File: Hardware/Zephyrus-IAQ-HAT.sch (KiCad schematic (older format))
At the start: 8 parts, among them J1 Conn_02x20_Odd_Even__Rpi, J2 USART, U3 BSS138

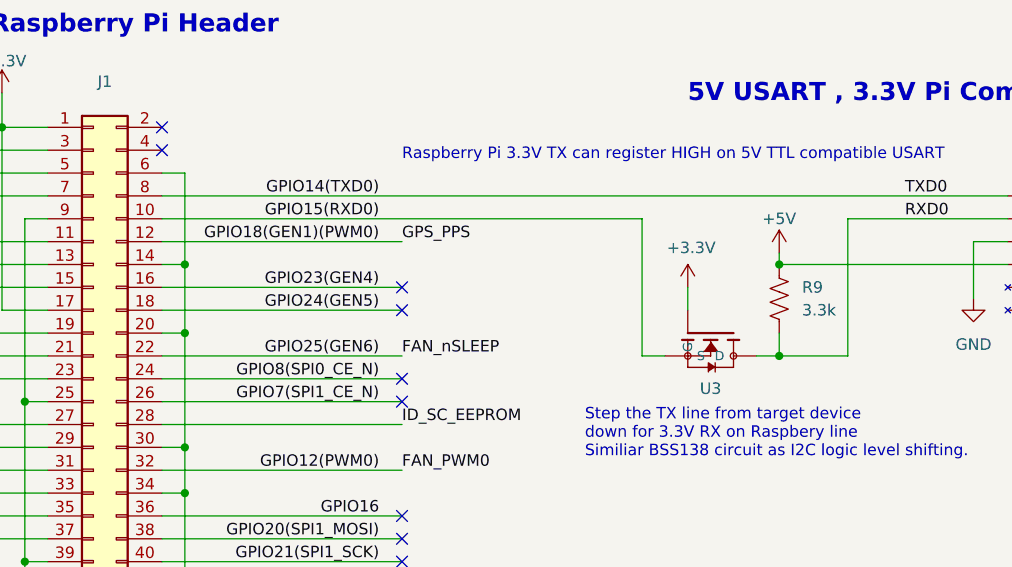
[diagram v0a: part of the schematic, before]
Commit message: Add Pull-Up to UART line.
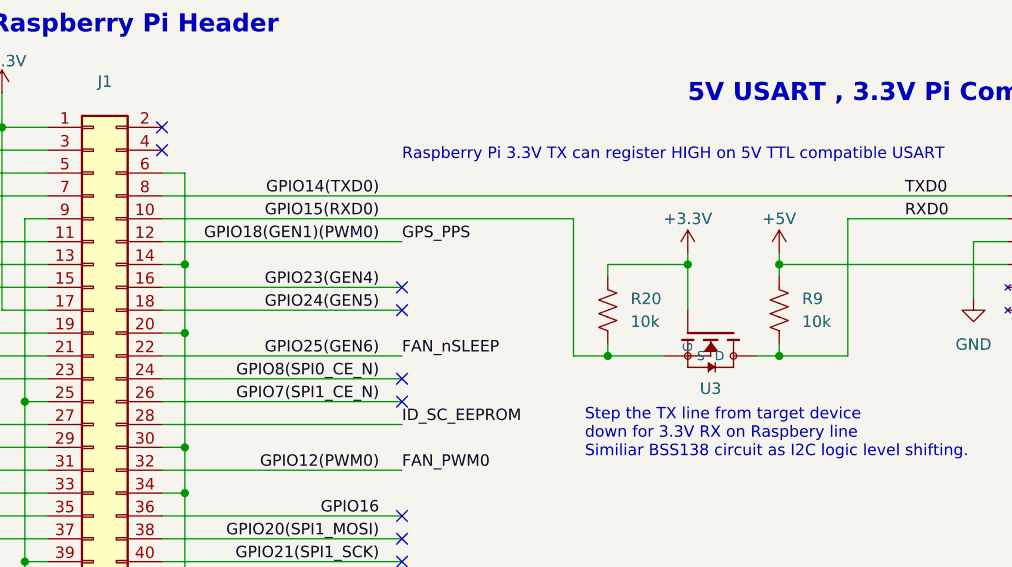
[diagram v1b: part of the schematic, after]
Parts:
- added R20: 10k, Resistor_SMD:R_0805_2012Metric, symbol zephyrus_iaq:R_US
- R9: value 3.3k -> 10k
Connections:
- wire segments 81 -> 87
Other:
- moved on the sheet: R9
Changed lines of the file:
@@
 Text Notes 2000 750  0    79   ~ 16
 Raspberry Pi Header
-Wire Wire Line
-	5050 1850 5050 1950
 $Comp
 L zephyrus_iaq:BSS138 U?
@@
 L zephyrus_iaq:R_US R?
 U 1 1 5DE9F972
-P 5450 1900
+P 5450 1950
 AR Path="/5DB861AF/5DE9F972" Ref="R?"  Part="1"
 AR Path="/5DE9F972" Ref="R9"  Part="1"
-F 0 "R9" H 5550 1950 50  0000 L CNN
-F 1 "3.3k" H 5550 1850 50  0000 L CNN
-F 2 "Resistor_SMD:R_0805_2012Metric" V 5490 1890 50  0001 C CNN
-F 3 "~" H 5450 1900 50  0001 C CNN
-	1    5450 1900
-	1    0    0    -1
-$EndComp
-Wire Wire Line
-	4850 2150 4950 2150
-Wire Wire Line
-	5350 2150 5450 2150
-Wire Wire Line
-	5450 2150 5450 2050
+F 0 "R9" H 5550 2000 50  0000 L CNN
+F 1 "10k" H 5550 1900 50  0000 L CNN
+F 2 "Resistor_SMD:R_0805_2012Metric" V 5490 1940 50  0001 C CNN
+F 3 "~" H 5450 1950 50  0001 C CNN
+	1    5450 1950
+	1    0    0    -1
+$EndComp
 $Comp
 L zephyrus_iaq:+3.3V #PWR?
 U 1 1 5DE9F969
-P 5050 1850
+P 5050 1700
 AR Path="/5DB861AF/5DE9F969" Ref="#PWR?"  Part="1"
 AR Path="/5DE9F969" Ref="#PWR0109"  Part="1"
-F 0 "#PWR0109" H 5050 1700 50  0001 C CNN
-F 1 "+3.3V" H 5065 2023 50  0000 C CNN
-F 2 "" H 5050 1850 50  0001 C CNN
-F 3 "" H 5050 1850 50  0001 C CNN
-	1    5050 1850
+F 0 "#PWR0109" H 5050 1550 50  0001 C CNN
+F 1 "+3.3V" H 5050 1850 50  0000 C CNN
+F 2 "" H 5050 1700 50  0001 C CNN
+F 3 "" H 5050 1700 50  0001 C CNN
+	1    5050 1700
 	1    0    0    -1
 $EndComp
@@
 $EndComp
 Wire Wire Line
-	5450 2150 5750 2150
-Wire Wire Line
 	5750 2150 5750 1550
-Connection ~ 5450 2150
 Wire Wire Line
 	5750 1550 6450 1550
@@
 Wire Wire Line
 	5450 1700 5450 1750
-Connection ~ 5450 1750
-Wire Wire Line
-	4850 1550 4850 2150
-Wire Wire Line
-	2750 1550 4850 1550
 Wire Wire Line
 	2750 1450 6450 1450
@@
 	1    0    0    -1
 $EndComp
+$Comp
+L zephyrus_iaq:R_US R?
+U 1 1 5DD3B4E5
+P 4700 1950
+AR Path="/5DB861AF/5DD3B4E5" Ref="R?"  Part="1"
+AR Path="/5DD3B4E5" Ref="R20"  Part="1"
+F 0 "R20" H 4800 2000 50  0000 L CNN
+F 1 "10k" H 4800 1900 50  0000 L CNN
+F 2 "Resistor_SMD:R_0805_2012Metric" V 4740 1940 50  0001 C CNN
+F 3 "~" H 4700 1950 50  0001 C CNN
+	1    4700 1950
+	1    0    0    -1
+$EndComp
+Wire Wire Line
+	2750 1550 4550 1550
+Wire Wire Line
+	4550 2150 4550 1550
+Wire Wire Line
+	5050 1700 5050 1750
+Wire Wire Line
+	4700 1750 5050 1750
+Connection ~ 5050 1750
+Wire Wire Line
+	5050 1750 5050 1950
+Wire Wire Line
+	4550 2150 4700 2150
+Wire Wire Line
+	5350 2150 5450 2150
+Wire Wire Line
+	4700 2100 4700 2150
+Connection ~ 4700 2150
+Wire Wire Line
+	4700 2150 4950 2150
+Wire Wire Line
+	4700 1800 4700 1750
+Wire Wire Line
+	5450 1800 5450 1750
+Connection ~ 5450 1750
+Wire Wire Line
+	5450 2100 5450 2150
+Connection ~ 5450 2150
+Wire Wire Line
+	5450 2150 5750 2150
 $EndSCHEMATC

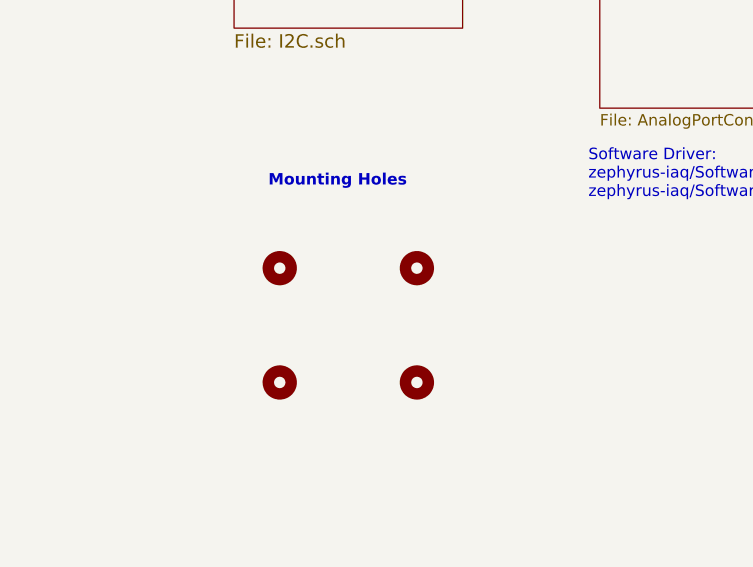
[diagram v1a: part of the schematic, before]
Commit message: Update PCB to latest schematic changes.
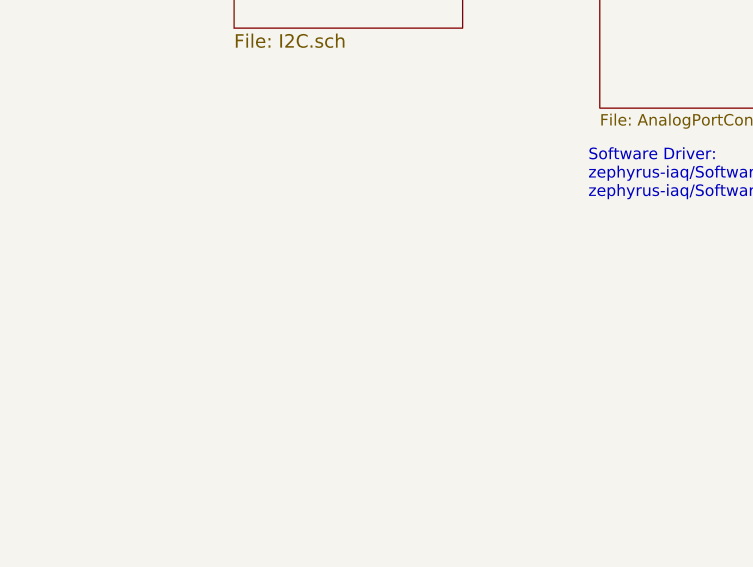
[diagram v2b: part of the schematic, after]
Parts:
- removed MK1, MK2, MK3, MK4: M2.5, MountingHole:MountingHole_2.7mm_M2.5, symbol zephyrus_iaq:Mounting-Hole-Mechanical
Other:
- note removed: "Mounting Holes"
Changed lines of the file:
@@
 Wire Wire Line
 	2750 1450 6450 1450
-Text Notes 1550 6050 0    50   ~ 10
-Mounting Holes
-$Comp
-L zephyrus_iaq:Mounting-Hole-Mechanical MK1
-U 1 1 5DD01DA5
-P 1600 6300
-AR Path="/5DD01DA5" Ref="MK1"  Part="1"
-AR Path="/5DAFB35B/5DD01DA5" Ref="MK?"  Part="1"
-F 0 "MK1" H 1700 6246 50  0001 L CNN
-F 1 "M2.5" H 1700 6155 50  0001 L CNN
-F 2 "MountingHole:MountingHole_2.7mm_M2.5" H 1600 6300 50  0001 C CNN
-F 3 "" H 1600 6300 50  0001 C CNN
-	1    1600 6300
-	1    0    0    -1
-$EndComp
-$Comp
-L zephyrus_iaq:Mounting-Hole-Mechanical MK3
-U 1 1 5DD01D9F
-P 1600 6800
-AR Path="/5DD01D9F" Ref="MK3"  Part="1"
-AR Path="/5DAFB35B/5DD01D9F" Ref="MK?"  Part="1"
-F 0 "MK3" H 1700 6746 50  0001 L CNN
-F 1 "M2.5" H 1700 6655 50  0001 L CNN
-F 2 "MountingHole:MountingHole_2.7mm_M2.5" H 1600 6800 50  0001 C CNN
-F 3 "" H 1600 6800 50  0001 C CNN
-	1    1600 6800
-	1    0    0    -1
-$EndComp
-$Comp
-L zephyrus_iaq:Mounting-Hole-Mechanical MK2
-U 1 1 5DD01D99
-P 2200 6300
-AR Path="/5DD01D99" Ref="MK2"  Part="1"
-AR Path="/5DAFB35B/5DD01D99" Ref="MK?"  Part="1"
-F 0 "MK2" H 2300 6246 50  0001 L CNN
-F 1 "M2.5" H 2300 6155 50  0001 L CNN
-F 2 "MountingHole:MountingHole_2.7mm_M2.5" H 2200 6300 50  0001 C CNN
-F 3 "" H 2200 6300 50  0001 C CNN
-	1    2200 6300
-	1    0    0    -1
-$EndComp
-$Comp
-L zephyrus_iaq:Mounting-Hole-Mechanical MK4
-U 1 1 5DD01D93
-P 2200 6800
-AR Path="/5DD01D93" Ref="MK4"  Part="1"
-AR Path="/5DAFB35B/5DD01D93" Ref="MK?"  Part="1"
-F 0 "MK4" H 2300 6746 50  0001 L CNN
-F 1 "M2.5" H 2300 6655 50  0001 L CNN
-F 2 "MountingHole:MountingHole_2.7mm_M2.5" H 2200 6800 50  0001 C CNN
-F 3 "" H 2200 6800 50  0001 C CNN
-	1    2200 6800
-	1    0    0    -1
-$EndComp
 Text Notes 9600 1300 2    79   ~ 16
 Raspberry Pi HAT\nRequirements:\nEEPROM\n\n

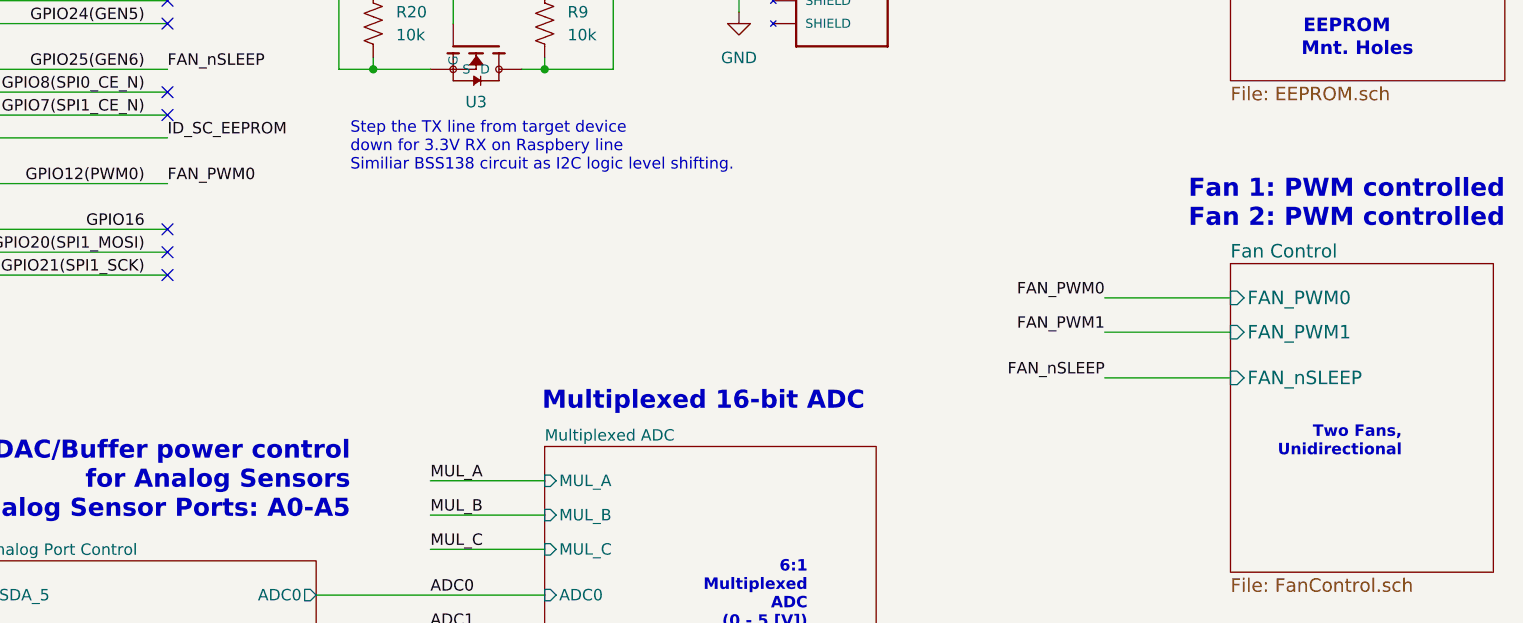
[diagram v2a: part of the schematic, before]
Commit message: Fix fan control.
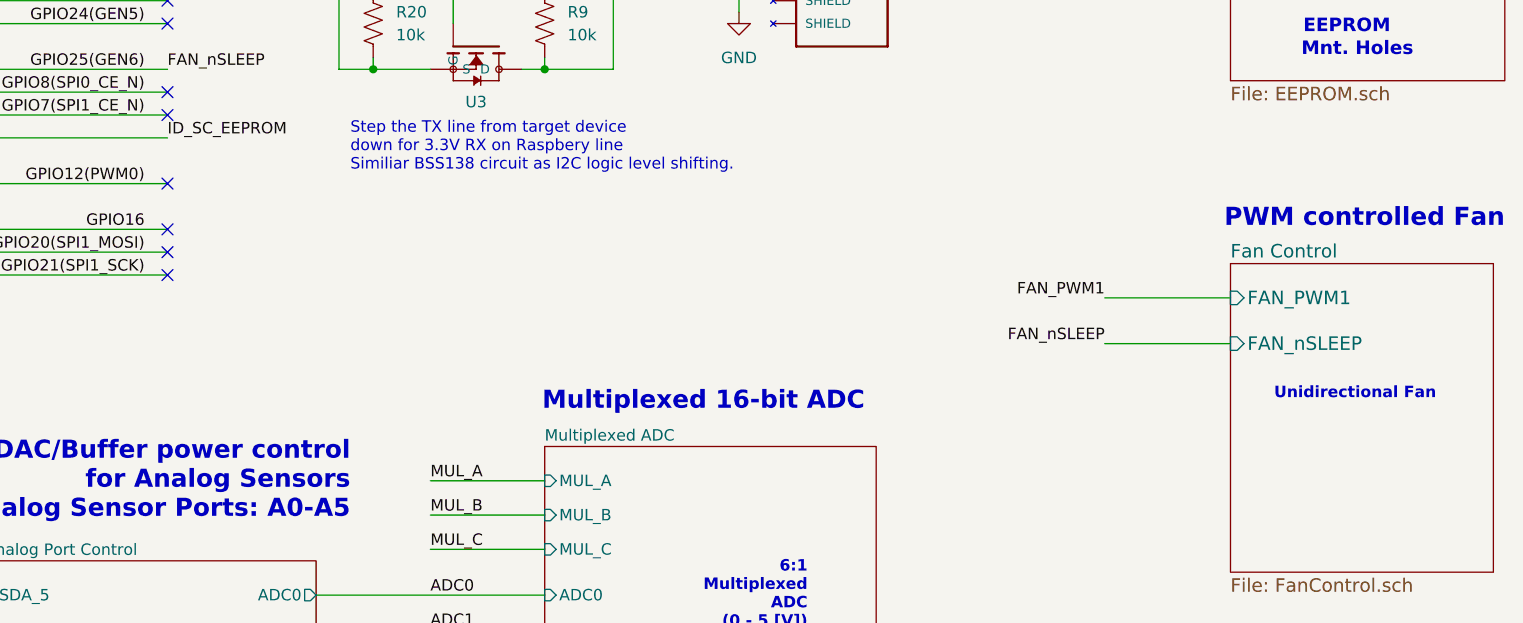
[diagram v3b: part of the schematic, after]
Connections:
- net labels removed: FAN_PWM0
- wire segments 87 -> 86
- no-connect marks 17 -> 18
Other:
- note added: "PWM controlled Fan\n"
- note added: "Unidirectional Fan\n"
- note removed: "Fan 1: PWM controlled\nFan 2: PWM controlled"
- note removed: "Two Fans, \nUnidirectional"
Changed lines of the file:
@@
 Text Label 1100 1850 2    50   ~ 0
 MUL_C
-Text Label 7900 3150 2    50   ~ 0
-FAN_PWM0
-Text Label 7900 3300 2    50   ~ 0
-FAN_PWM1
-Text Label 7900 3500 2    50   ~ 0
+Text Label 7900 3350 2    50   ~ 0
 FAN_nSLEEP
 Text Label 3800 2150 0    50   ~ 0
 FAN_nSLEEP
-Text Label 3800 2650 0    50   ~ 0
-FAN_PWM0
 Text Label 1100 2750 2    50   ~ 0
 FAN_PWM1
@@
 F0 "Fan Control" 59
 F1 "FanControl.sch" 59
-F2 "FAN_PWM0" I L 8450 3150 59
-F3 "FAN_PWM1" I L 8450 3300 59
-F4 "FAN_nSLEEP" I L 8450 3500 59
+F2 "FAN_PWM1" I L 8450 3150 59
+F3 "FAN_nSLEEP" I L 8450 3350 59
 $EndSheet
 Wire Wire Line
@@
 Wire Wire Line
 	1400 4800 950  4800
-Text Notes 9200 3850 2    50   ~ 10
-Two Fans, \nUnidirectional
+Text Notes 9350 3600 2    50   ~ 10
+Unidirectional Fan\n
 Text Notes 6600 4600 2    50   ~ 10
 6:1\nMultiplexed\nADC\n (0 - 5 [V])
@@
 Text Notes 2450 4000 2    79   ~ 16
 I2C Connectors\nand\nI2C Logic Level Conversion
-Text Notes 9650 2850 2    79   ~ 16
-Fan 1: PWM controlled\nFan 2: PWM controlled
 Wire Wire Line
 	7900 3150 8450 3150
 Wire Wire Line
-	8450 3300 7900 3300
-Wire Wire Line
-	8450 3500 7900 3500
+	8450 3350 7900 3350
 Wire Wire Line
 	4450 5400 5450 5400
@@
 Wire Wire Line
 	5450 2150 5750 2150
+Text Notes 9650 2850 2    79   ~ 16
+ PWM controlled Fan\n
+Text Label 7900 3150 2    50   ~ 0
+FAN_PWM1
+NoConn ~ 3800 2650
 $EndSCHEMATC
